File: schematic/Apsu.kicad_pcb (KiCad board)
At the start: 2 copper layers, 76.7 x 52.7 mm, 63 parts, among them J1 Conn_02x03_Odd_Even, J10 Conn_01x03, J11 Conn_01x03, J12 Conn_01x02_Male, J13 Conn_01x02, J2 Conn_02x05_Odd_Even, J3 Conn_02x06_Odd_Even, J4 Conn_01x05, J5 Conn_01x05, J6 Conn_01x03, J7 Conn_01x02, J8 Conn_01x03_Female, J9 Conn_01x03, U1 ESP32-WROOM-32, U2 PCA9685PW, U3 ADS1015IDGS, U4 FAN4860UC5X, U5 LIS2MDL, U6 LSM6DSOX, U7 BME280, U8 SP3485CN

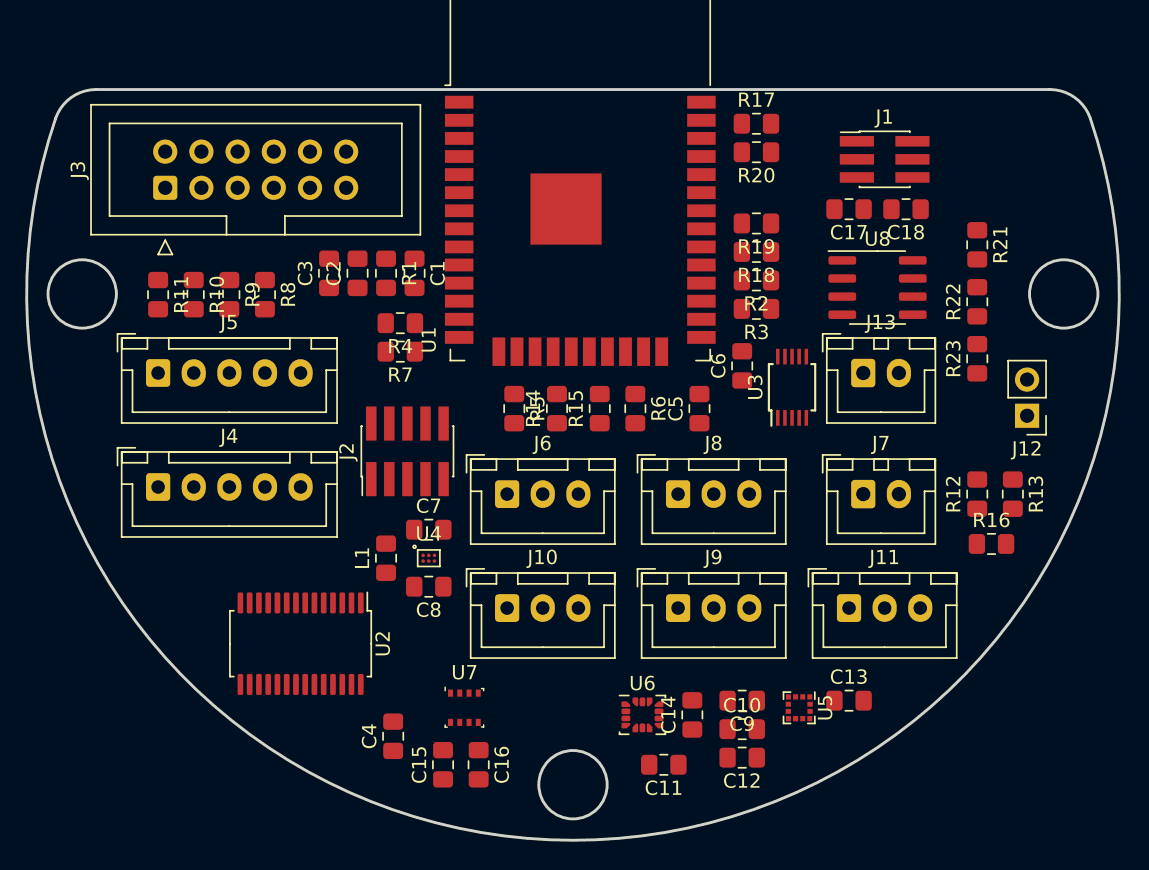
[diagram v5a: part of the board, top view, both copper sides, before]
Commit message: new components on pcb
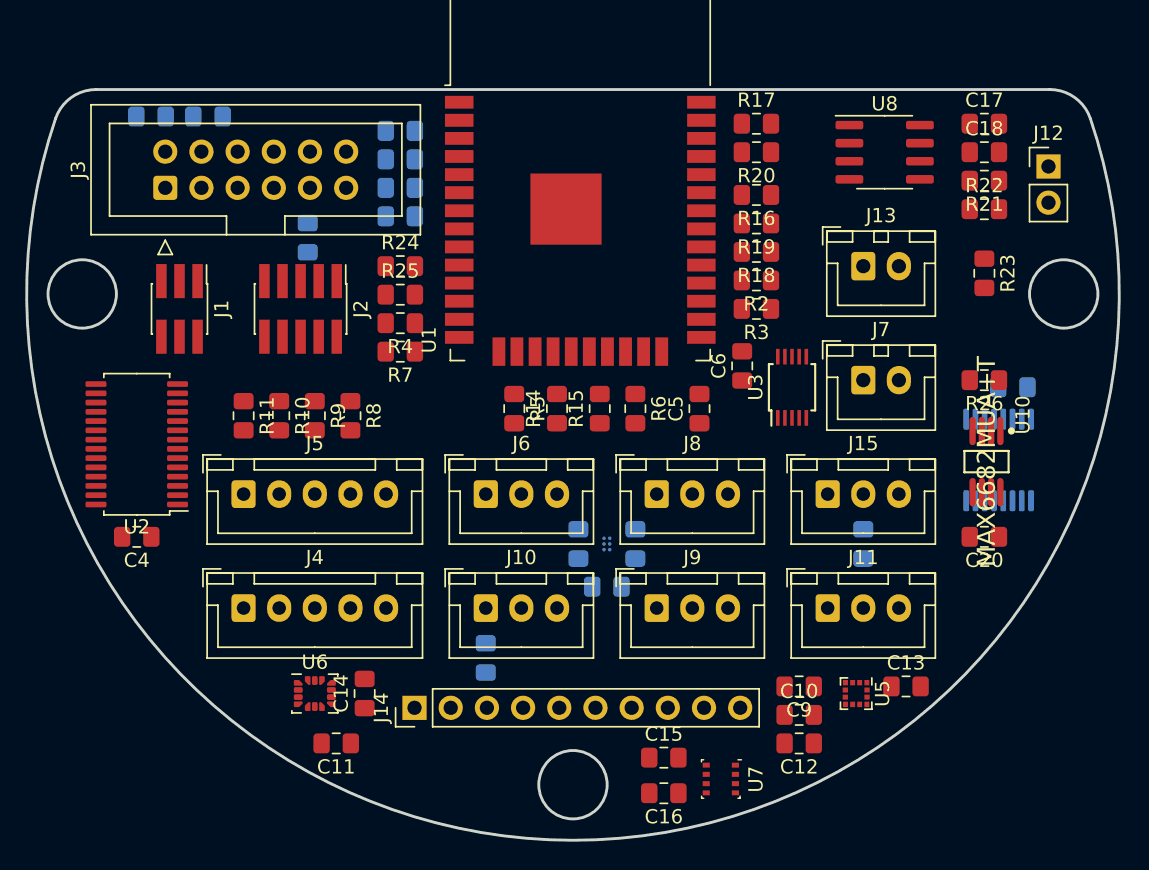
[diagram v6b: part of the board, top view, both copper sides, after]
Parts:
- added C19: 0.1uF, Capacitor_SMD:C_0805_2012Metric_Pad1.15x1.40mm_HandSolder, B.Cu at (184.0, 101.0)
- added C20: 0.1uF, Capacitor_SMD:C_0805_2012Metric_Pad1.15x1.40mm_HandSolder, F.Cu at (182.0, 111.5)
- added C21: 0.1uF, Capacitor_SMD:C_0805_2012Metric_Pad1.15x1.40mm_HandSolder, B.Cu at (173.5, 112.0)
- added C22: 0.1uF, Capacitor_SMD:C_0805_2012Metric_Pad1.15x1.40mm_HandSolder, B.Cu at (127.5, 82.0)
- added C23: 10uF, Capacitor_SMD:C_0805_2012Metric_Pad1.15x1.40mm_HandSolder, B.Cu at (123.5, 82.0)
- added J14: Conn_01x10_Male, Connector_PinHeader_2.54mm:PinHeader_1x10_P2.54mm_Vertical, F.Cu at (142.0, 123.5)
- added J15: Conn_01x03_Female, Connector_JST:JST_XH_B3B-XH-A_1x03_P2.50mm_Vertical, F.Cu at (171.0, 108.5)
- added R24: 10k, Resistor_SMD:R_0805_2012Metric_Pad1.15x1.40mm_HandSolder, F.Cu at (141.0, 92.5)
- added R25: 10k, Resistor_SMD:R_0805_2012Metric_Pad1.15x1.40mm_HandSolder, F.Cu at (141.0, 94.5)
- added R26: 287, Resistor_SMD:R_0805_2012Metric_Pad1.15x1.40mm_HandSolder, F.Cu at (182.0, 100.5)
- added U10: MAX6682MUA+T, MAX6682:Maxim-MAX6682MUA+T-Level_A, F.Cu at (182.2, 106.2)
- added U9: MC74HC138A, Package_SO:TSSOP-16_4.4x5mm_P0.65mm, B.Cu at (183.0, 106.1)
- C1, C2, C3, C7, C8, L1, R1, U4: moved to B.Cu
- R12: value 30900 -> 100k; moved to B.Cu
- R13: value 9530 -> 5k; moved to B.Cu
- R16: value R -> 10k
- moved J1 50.6 mm to (125.5, 95.5), turned to 270 degrees
- moved R12 50.3 mm to (134.5, 90.5)
- moved R13 38.7 mm to (147.0, 120.0), turned to 90 degrees
- moved R16 29.5 mm to (166.0, 87.5), turned to 180 degrees
- moved C11 23.0 mm to (136.5, 126.0)
- moved C14 23.0 mm to (138.5, 122.5)
- moved U6 23.0 mm to (135.0, 122.5)
- moved C4 22.8 mm to (122.5, 111.5), turned to 180 degrees
- moved U7 18.7 mm to (163.5, 128.5), turned to 270 degrees
- moved U2 18.1 mm to (122.5, 105.0), turned to 180 degrees
- moved J12 17.6 mm to (186.5, 85.5), turned to 0 degrees
- moved L1 15.6 mm to (155.5, 115.0), turned to 0 degrees
- moved C15 15.5 mm to (159.5, 127.0), turned to 0 degrees
- moved C7 14.5 mm to (157.5, 112.0), turned to 90 degrees
- moved C16 13.2 mm to (159.5, 129.5), turned to 180 degrees
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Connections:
- net SIS_water renamed SIS_water_0
- J7 pad 2: water_temp -> GND
- R12 pad 1: +12V -> GND
- R12 pad 2: BAT_volt -> SPI-MISO
- R13 pad 1: BAT_volt -> +3V3
- R13 pad 2: GND -> DS18B20
- R16 pad 1: Net-(J7-Pad1) -> GND
- R16 pad 2: +3V3 -> SPI-SS0
- R2 pad 2: I2C-SCL -> I2C-SDA
- R3 pad 2: I2C-SDA -> I2C-SCL
- U1 pad 24: Net-(U1-Pad24) -> IO2
- U2 pad 10: Net-(U2-Pad10) -> PWM_custom_0
- U2 pad 11: Net-(U2-Pad11) -> PWM_custom_1
- U2 pad 12: Net-(U2-Pad12) -> PWM_custom_2
- U3 pad 5: water_temp -> water_pressure
- U3 pad 6: water_pressure -> ADC_custom_0
- U3 pad 7: BAT_volt -> ADC_custom_1

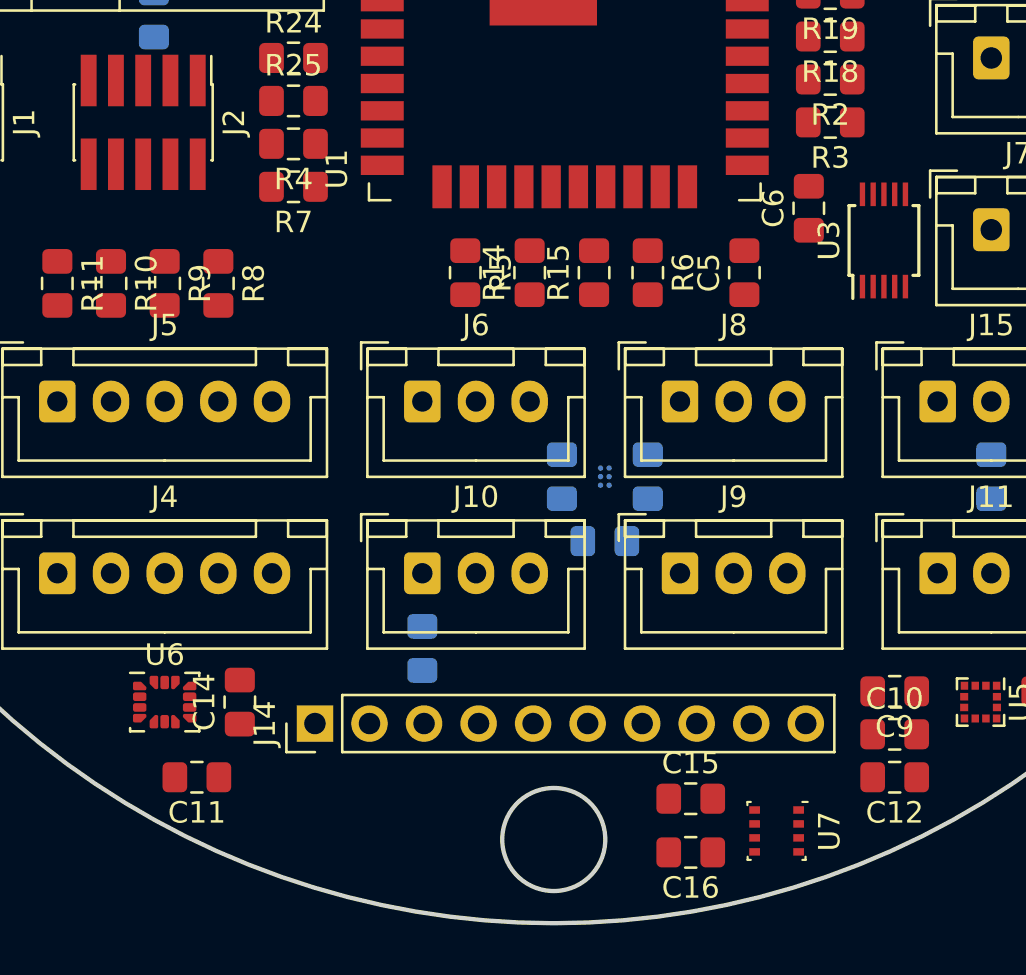
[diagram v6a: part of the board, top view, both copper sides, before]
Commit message: JTAG anti-ring resistors
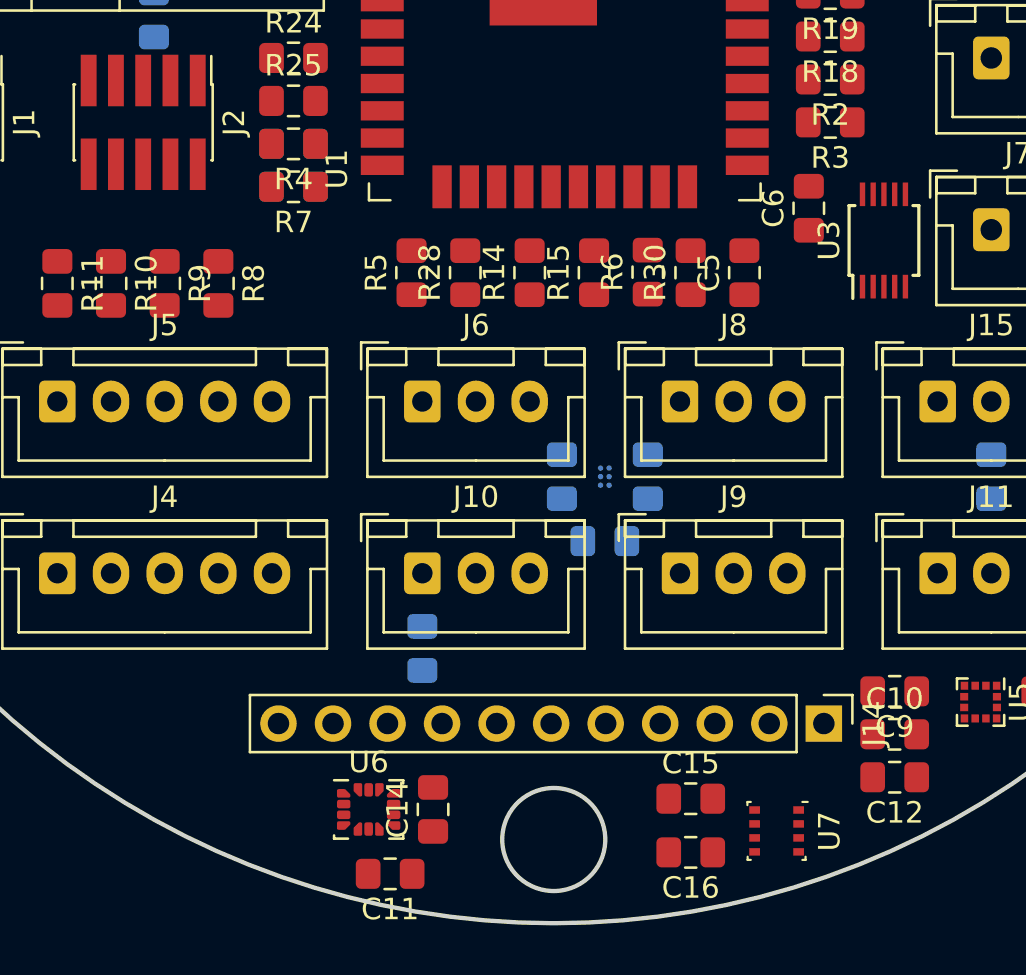
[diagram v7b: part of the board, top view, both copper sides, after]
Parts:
- added R27: 100, Resistor_SMD:R_0805_2012Metric_Pad1.15x1.40mm_HandSolder, B.Cu at (141.0, 98.5)
- added R28: 100, Resistor_SMD:R_0805_2012Metric_Pad1.15x1.40mm_HandSolder, F.Cu at (149.0, 102.5)
- added R29: 100, Resistor_SMD:R_0805_2012Metric_Pad1.15x1.40mm_HandSolder, B.Cu at (141.0, 96.5)
- added R30: 100, Resistor_SMD:R_0805_2012Metric_Pad1.15x1.40mm_HandSolder, F.Cu at (159.5, 102.5)
- J14: value Conn_01x10_Male -> Conn_01x11_Male; footprint Connector_PinHeader_2.54mm:PinHeader_1x10_P2.54mm_Vertical -> Connector_PinHeader_2.54mm:PinHeader_1x11_P2.54mm_Vertical
- moved J14 23.7 mm to (165.7, 123.5), turned to 270 degrees
- moved U6 10.7 mm to (144.5, 127.5)
- moved C14 10.3 mm to (147.5, 127.5)
- moved C11 10.1 mm to (145.5, 130.5)
- moved R5 2.50 mm to (146.5, 102.5), turned to 90 degrees
- turned R6 to 90 degrees
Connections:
- J14 pad 2: GND -> +3V3
- J14 pad 3: +3V3 -> Sensor_VP
- J14 pad 4: +3V3 -> Sensor_VN
- U1 pad 13: JTAG-TMS -> Net-(R29-Pad2)
- U1 pad 14: JTAG-TDI -> Net-(R27-Pad2)
- U1 pad 16: JTAG-TCK -> Net-(R28-Pad2)
- U1 pad 23: JTAG-TDO -> Net-(R30-Pad2)
- U1 pad 4: Net-(U1-Pad4) -> Sensor_VP
- U1 pad 5: Net-(U1-Pad5) -> Sensor_VN
- U2 pad 13: Net-(U2-Pad13) -> PWM_custom_3

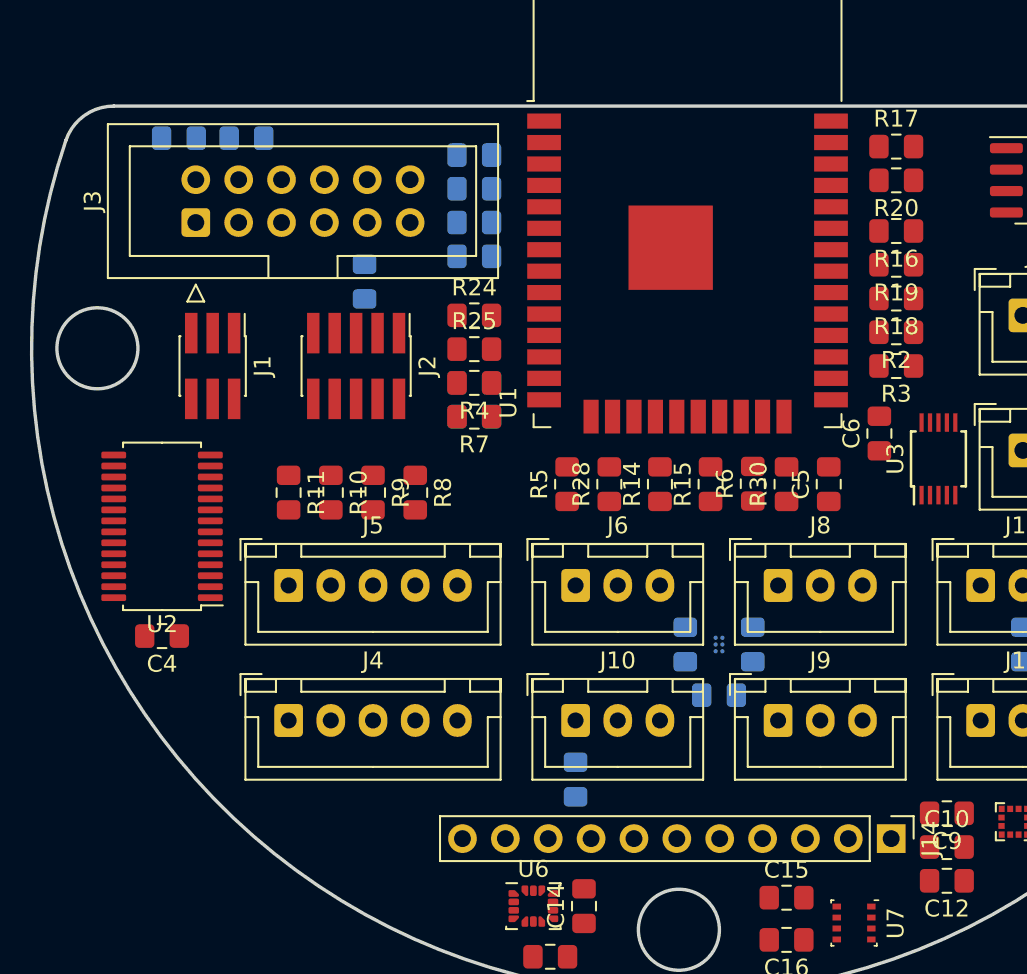
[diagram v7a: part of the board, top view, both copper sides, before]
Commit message: adjusted 1.27mm IDC and PCA9685 to correct footprint
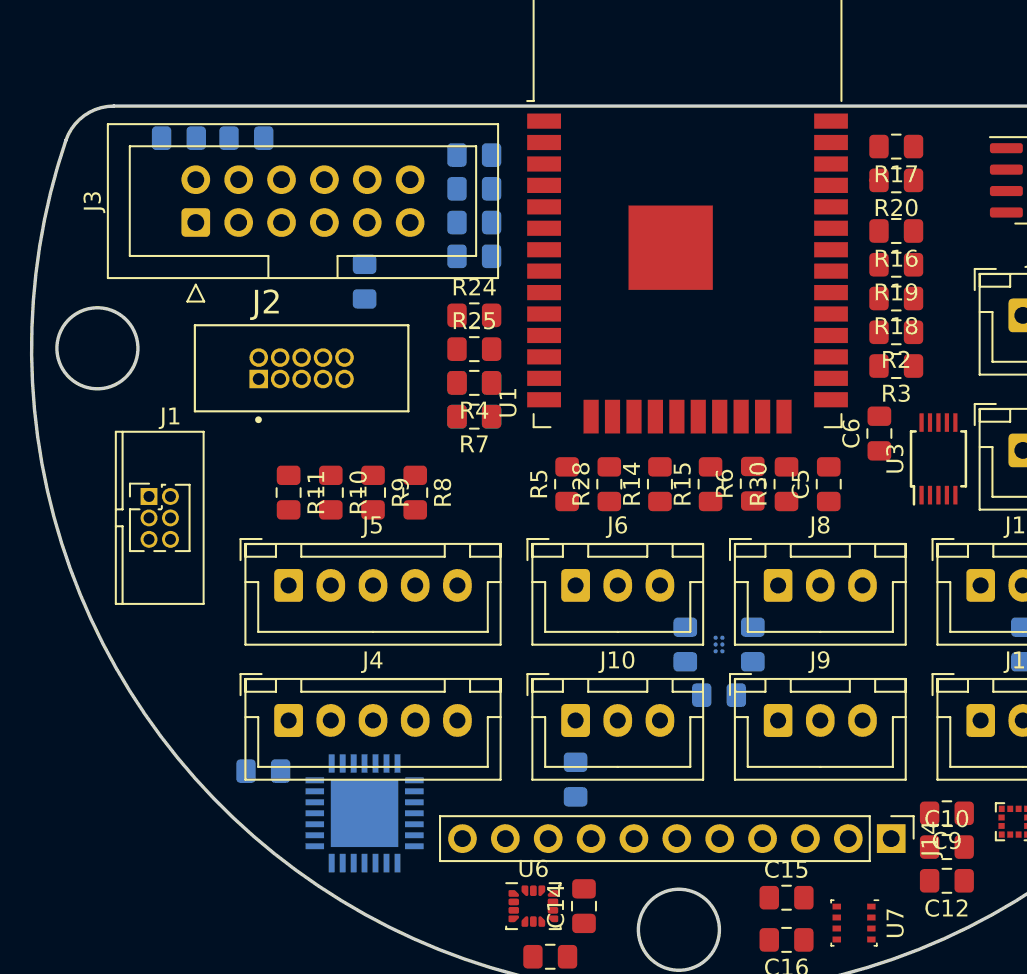
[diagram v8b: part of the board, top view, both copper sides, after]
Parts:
- C4: moved to B.Cu
- J1: footprint Connector_PinHeader_1.27mm:PinHeader_2x03_P1.27mm_Vertical_SMD -> Apsu:PinHeader_2x03_P1.27mm_Vertical_IDC
- J2: footprint Connector_PinHeader_1.27mm:PinHeader_2x05_P1.27mm_Vertical_SMD -> Apsu:10pin1.27mmIDC
- U2: footprint Package_SO:TSSOP-28_4.4x9.7mm_P0.65mm -> PCA9685:NXP_Semiconductors-SOT788-1-02_2016-0-MFG; moved to B.Cu
- moved U2 20.8 mm to (134.5, 122.0), turned to 270 degrees
- moved C4 10.0 mm to (128.5, 119.5), turned to 0 degrees
- moved J1 9.53 mm to (122.4, 104.5), turned to 0 degrees
- moved J2 3.23 mm to (130.8, 95.6), turned to 0 degrees
- turned R17 to 180 degrees
